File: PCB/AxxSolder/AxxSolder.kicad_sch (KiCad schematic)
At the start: 86 parts, among them IC1 LTC4440AHMS8E-5#PBF, IC2 STM32G431KBT6, IC3 TMP236AQDBZRQ1, IC4 OPA2333AIDRBR, IC5 STM32G431KBT6, J1 Conn_01x07_Male, J4 Conn_01x07_Male, Q2 2N7002NXAKR, U1 PEC11L-4220F-S0015, U2 BSC014N04LS

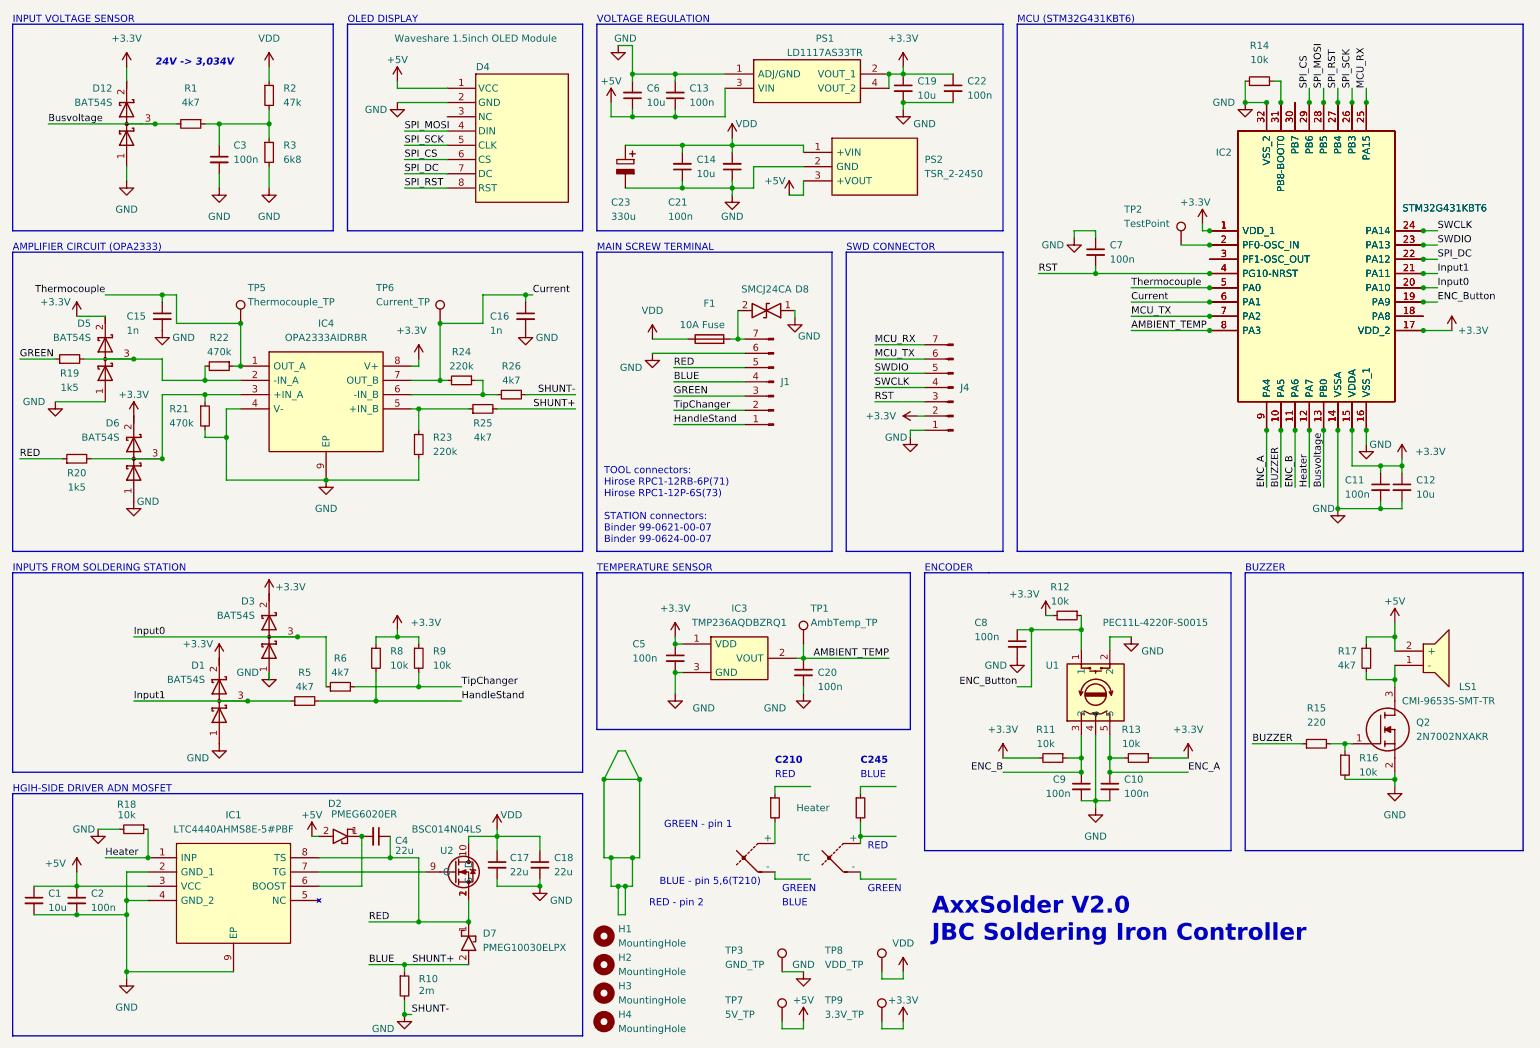
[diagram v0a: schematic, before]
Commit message: Change to new, more cost effective VCC->5V DC/DC solution, update to AxxSolder V2.1
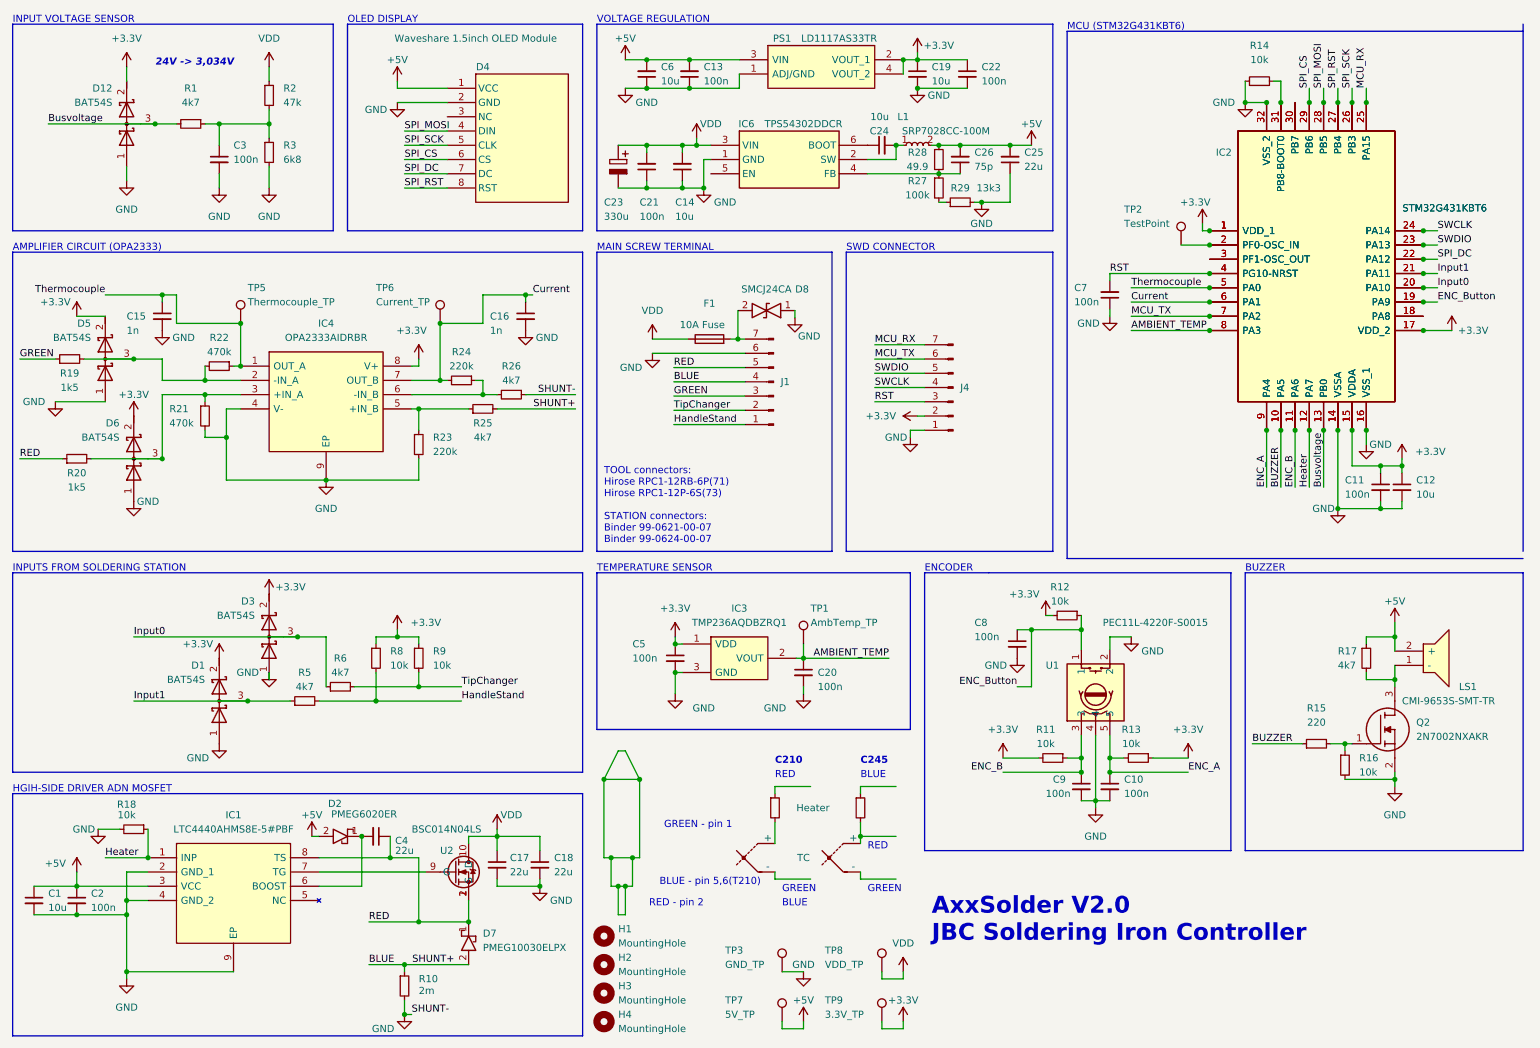
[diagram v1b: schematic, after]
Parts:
- removed PS2: TSR_2-2450, TSR-2, symbol TSR_2-2450:TSR_2-2450
- added C24: 10u, Capacitor_SMD:C_0805_2012Metric, symbol Device:C_Small
- added C25: 22u, Capacitor_SMD:C_0805_2012Metric, symbol Device:C_Small
- added C26: 75p, Capacitor_SMD:C_0805_2012Metric, symbol Device:C_Small
- added IC6: TPS54302DDCR, SOT95P280X110-6N, symbol TPS54302DDCR:TPS54302DDCR
- added L1: SRP7028CC-100M, INDPM7366X300N, symbol SRP7028CC-100M:SRP7028CC-100M
- added R27: 100k, Resistor_SMD:R_0805_2012Metric, symbol Device:R_Small
- added R28: 49.9, Resistor_SMD:R_0805_2012Metric, symbol Device:R_Small
- added R29: 13k3, Resistor_SMD:R_0805_2012Metric, symbol Device:R_Small
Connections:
- net +5V: now also C13.2, C6.2, C25.2, C26.2, L1.2, R28.1; no longer C13.1, C6.1
- net GND: now also C13.1, C6.1, C25.1, IC6.1 (GND), R29.2; no longer C13.2, C6.2
- net VDD: now also IC6.3 (VIN)
- new net: R27.2, R29.1
- new net: C24.2, IC6.2 (SW), L1.1
- new net: C26.1, IC6.4 (FB), R27.1, R28.2
- new net: C24.1, IC6.6 (BOOT)
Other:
- moved on the sheet: C13, C14, C19, C21, C22, C23, C6, C7, PS1

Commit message: Clean and structure schematic and update to AxxSolder V2.1
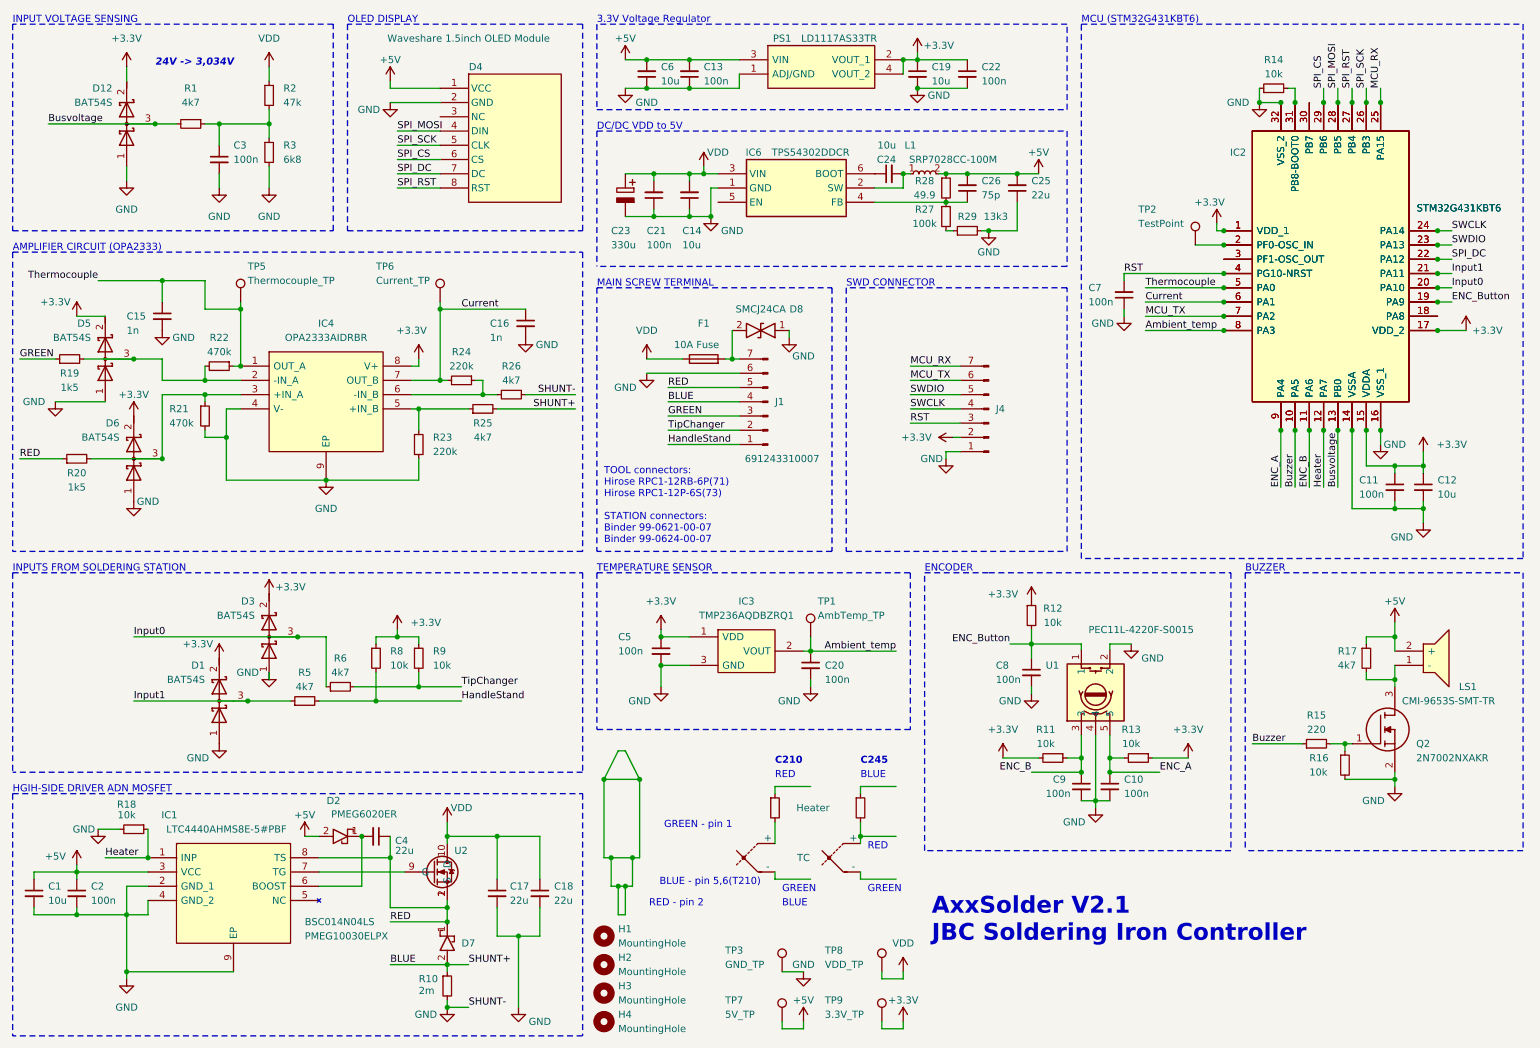
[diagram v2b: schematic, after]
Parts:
- J1: Manufacturer_Part_Number (none) -> 691243310007
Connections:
- net +3.3V: now also R12.1; no longer R12.2
- net ENC_Button: now also R12.2; no longer R12.1
- net AMBIENT_TEMP renamed Ambient_temp
- net BUZZER renamed Buzzer
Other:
- note added: "3.3V Voltage Regulator"
- note added: "AxxSolder V2.1 JBC Soldering Iron Controller"
- note added: "DC/DC VDD to 5V"
- note added: "INPUT VOLTAGE SENSING"
- note removed: "AxxSolder V2.0 JBC Soldering Iron Controller"
- note removed: "INPUT VOLTAGE SENSOR"
- note removed: "VOLTAGE REGULATION"
- moved on the sheet: C1, C11, C12, C14, C16, C17, C18, C2, C20, C21, C23, C24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

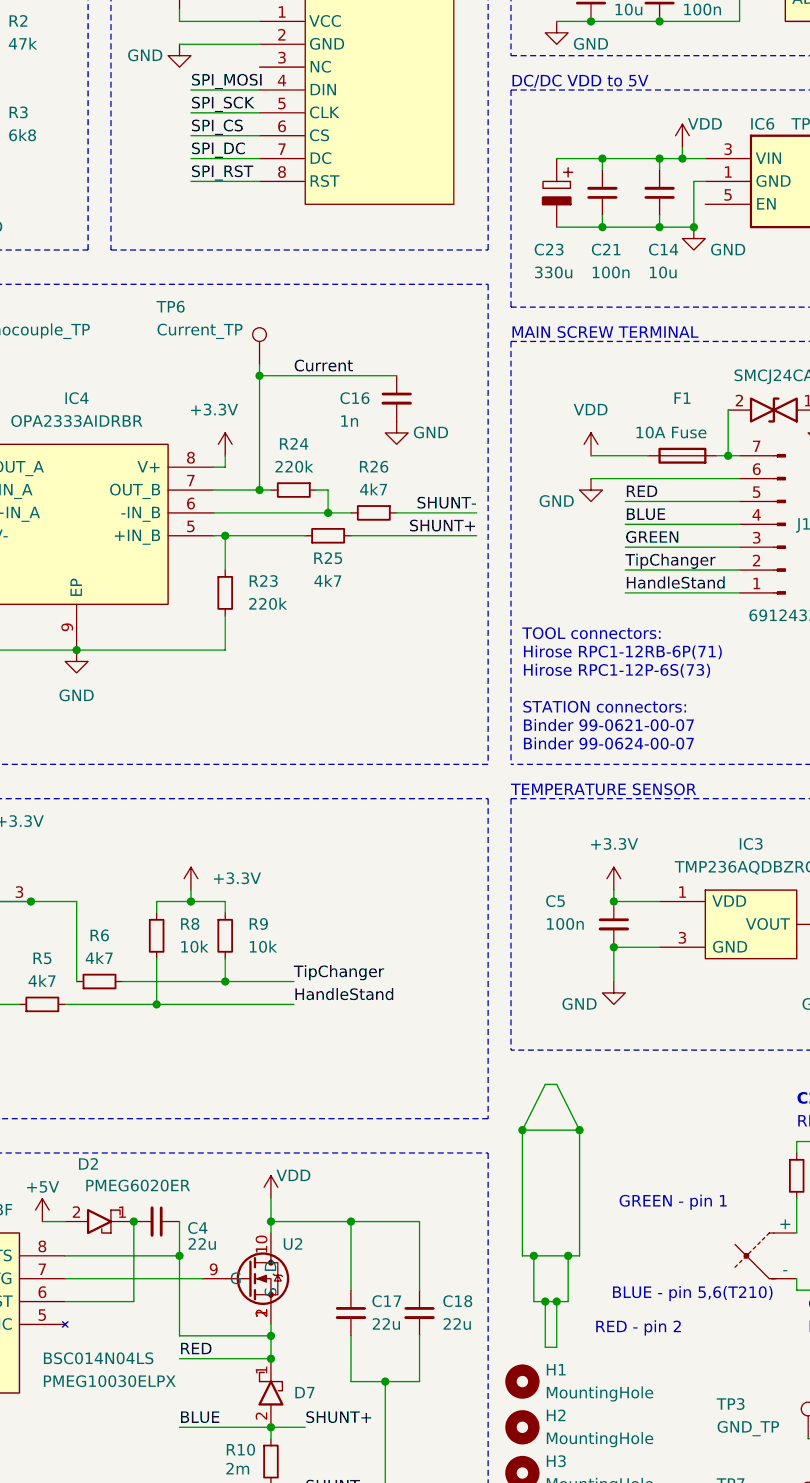
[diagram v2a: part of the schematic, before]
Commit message: Clean and structure PCB Layout and update to AxxSolder V2.1
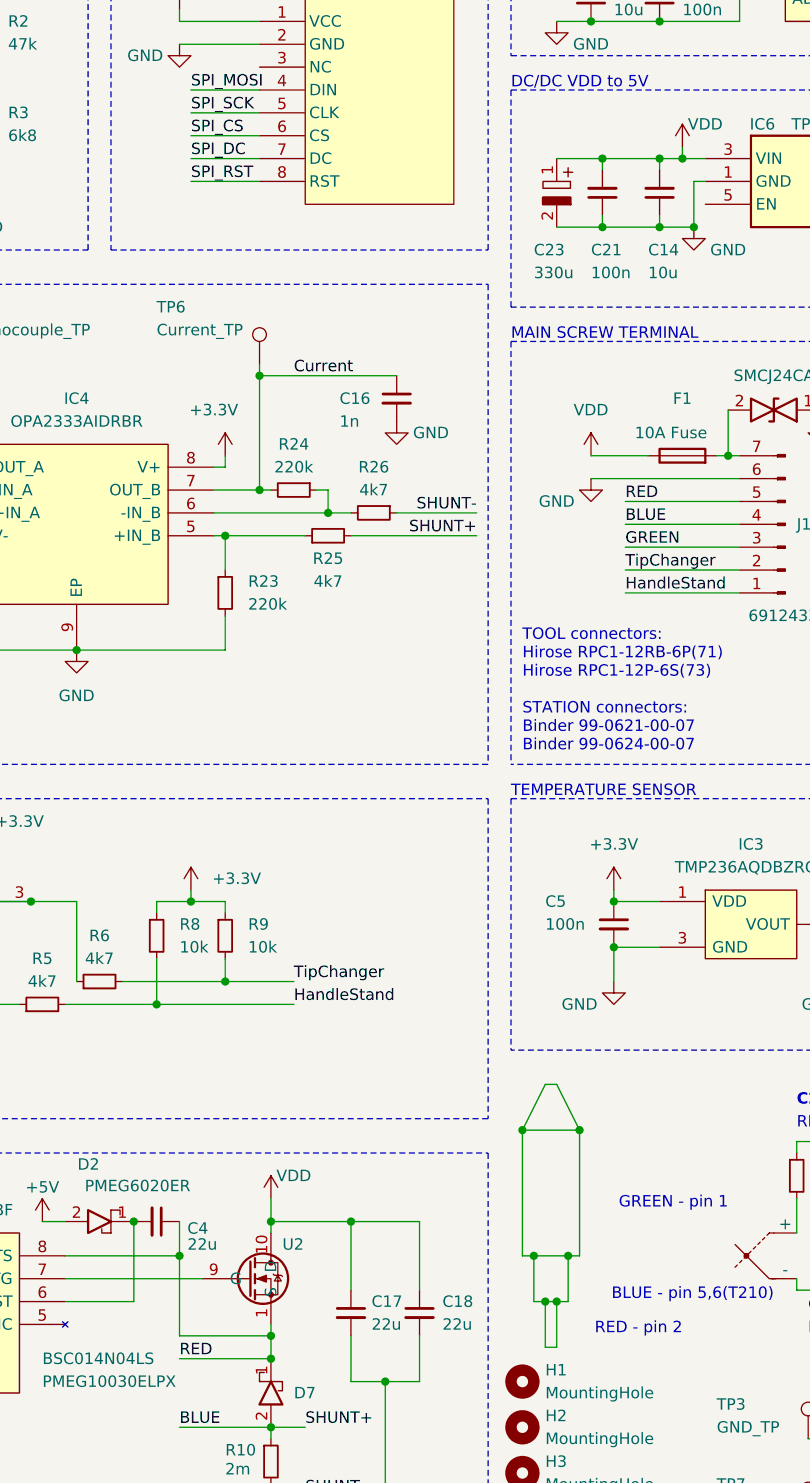
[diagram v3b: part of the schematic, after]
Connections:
- net GND: now also C23.2; no longer C23.
- net RED: no longer U2.2 (S), U2.3 (S)
- net VDD: now also C23.1; no longer C23.
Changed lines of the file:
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@@
     (pin "1")
     (pin "10")
-    (pin "2")
-    (pin "3")
     (pin "9")
     (instances
@@
       (effects (font (size 1.27 1.27)) (justify left) hide)
     )
-    (pin "")
-    (pin "")
-    (instances
-      (project "AxxSolder"
+    (pin "2")
+    (pin "1")
+    (instances
+      (project "AxxSolder"

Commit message: Change silkscreen to Input: 9-24V and optimize board layout
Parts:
- IC6: footprint SOT95P280X110-6N -> TPS54302DDCR:SOT95P280X110-6N
- L1: footprint INDPM7366X300N -> SRP7028CC-100M:INDPM7366X300N
- TP3: footprint testpin black 1mm:testpin black 1mm -> TestPoint:TestPoint_THTPad_D1.0mm_Drill0.5mm
- U1: footprint PEC11L4220FS0015 -> PEC11L-4220F-S0015:PEC11L4220FS0015
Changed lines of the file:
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@@
       (effects (font (size 1.27 1.27)))
     )
-    (property "Footprint" "INDPM7366X300N" (at 190.5 139.37 0)
+    (property "Footprint" "SRP7028CC-100M:INDPM7366X300N" (at 190.5 139.37 0)
       (effects (font (size 1.27 1.27)) (justify left top) hide)
     )
@@
       (effects (font (size 1.27 1.27)) (justify left))
     )
-    (property "Footprint" "testpin black 1mm:testpin black 1mm" (at 156.21 185.42 0)
+    (property "Footprint" "TestPoint:TestPoint_THTPad_D1.0mm_Drill0.5mm" (at 156.21 185.42 0)
       (effects (font (size 1.27 1.27)) hide)
     )
@@
       (effects (font (size 1.27 1.27)))
     )
-    (property "Footprint" "SOT95P280X110-6N" (at 163.83 138.1 0)
+    (property "Footprint" "TPS54302DDCR:SOT95P280X110-6N" (at 163.83 138.1 0)
       (effects (font (size 1.27 1.27)) (justify left top) hide)
     )
@@
       (effects (font (size 1.27 1.27)) (justify right))
     )
-    (property "Footprint" "PEC11L4220FS0015" (at 194.818 114.3 0)
+    (property "Footprint" "PEC11L-4220F-S0015:PEC11L4220FS0015" (at 194.818 114.3 0)
       (effects (font (size 1.27 1.27)) (justify left) hide)
     )
